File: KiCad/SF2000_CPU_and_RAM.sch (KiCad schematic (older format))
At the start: 5 parts, among them U10 IS61WV20488FBLL-10TLI, U11 IS61WV20488FBLL-10TLI, U12 IS61WV20488FBLL-10TLI, U13 IS61WV20488FBLL-10TLI, U9 68000D

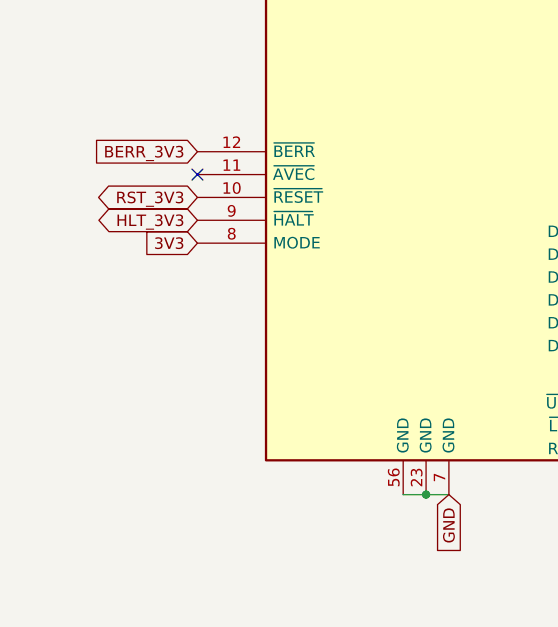
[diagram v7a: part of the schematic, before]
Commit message: Added resistor pack RN5 10k pull-ups for /WP, /AVEC, DONE, MODE
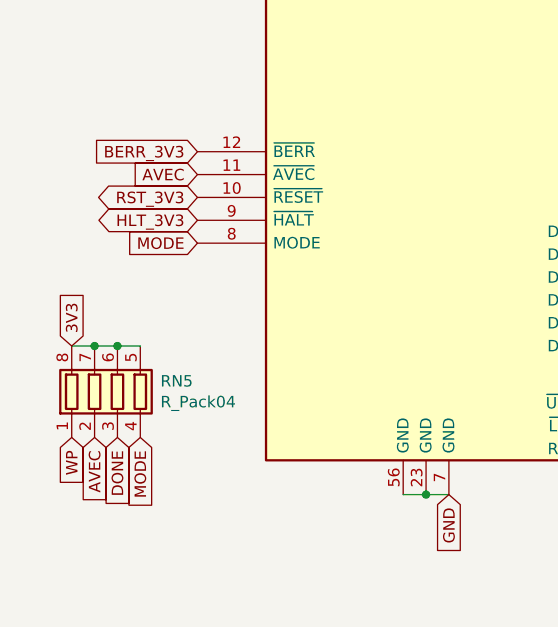
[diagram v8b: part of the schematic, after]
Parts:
- added RN5: R_Pack04, SF2000:RESCAF80P320X160X60-8N, symbol Device:R_Pack04
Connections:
- net 3V3: now also RN5.5 (R4.2), RN5.6 (R3.2), RN5.7 (R2.2), RN5.8 (R1.2); no longer U9.8 (MODE)
- net AVEC: now reaches U9.11 (~AVEC)
- net AVEC: now also RN5.2 (R2.1)
- new net DONE: RN5.3 (R3.1)
- new net MODE: RN5.4 (R4.1), U9.8 (MODE)
- new net WP: RN5.1 (R1.1)
- no-connect marks 2 -> 1
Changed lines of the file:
@@
 Text GLabel 3500 5900 2    50   Output ~ 0
 RW_3V3
-Text GLabel 1500 5000 0    50   Input ~ 0
+Text GLabel 950  5450 1    50   Input ~ 0
 3V3
 $Comp
@@
 Text GLabel 7500 1000 0    50   Input ~ 0
 A21_3V3
-NoConn ~ 1500 4700
 NoConn ~ 3500 1500
+$Comp
+L Device:R_Pack04 RN?
+U 1 1 62C74D68
+P 1150 5650
+AR Path="/62892CF3/62C74D68" Ref="RN?"  Part="1"
+AR Path="/621DFEC4/62C74D68" Ref="RN5"  Part="1"
+F 0 "RN5" H 1338 5696 50  0000 L CNN
+F 1 "R_Pack04" H 1338 5605 50  0000 L CNN
+F 2 "SF2000:RESCAF80P320X160X60-8N" V 1425 5650 50  0001 C CNN
+F 3 "~" H 1150 5650 50  0001 C CNN
+	1    1150 5650
+	1    0    0    -1
+$EndComp
+Wire Wire Line
+	950  5450 1050 5450
+Connection ~ 1050 5450
+Wire Wire Line
+	1050 5450 1150 5450
+Connection ~ 1150 5450
+Wire Wire Line
+	1150 5450 1250 5450
+Text GLabel 1500 5000 0    50   Input ~ 0
+MODE
+Text GLabel 1250 5850 3    50   Input ~ 0
+MODE
+Text GLabel 1500 4700 0    50   Input ~ 0
+AVEC
+Text GLabel 1050 5850 3    50   Input ~ 0
+AVEC
+Text GLabel 1150 5850 3    50   Input ~ 0
+DONE
+Text GLabel 950  5850 3    50   Input ~ 0
+WP
 $EndSCHEMATC
